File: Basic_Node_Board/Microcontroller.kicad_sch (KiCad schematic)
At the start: 30 parts, among them J1 Conn_01x02, J2 Conn_01x19_Socket, J3 Conn_01x19_Socket, J4 Conn_01x02_Pin, U2 ESP32-DEVKIT-C, U3 AP64060WU-7, U4 AP64060WU-7, U5 AP64060WU-7, U6 TJA1050T/CM,118

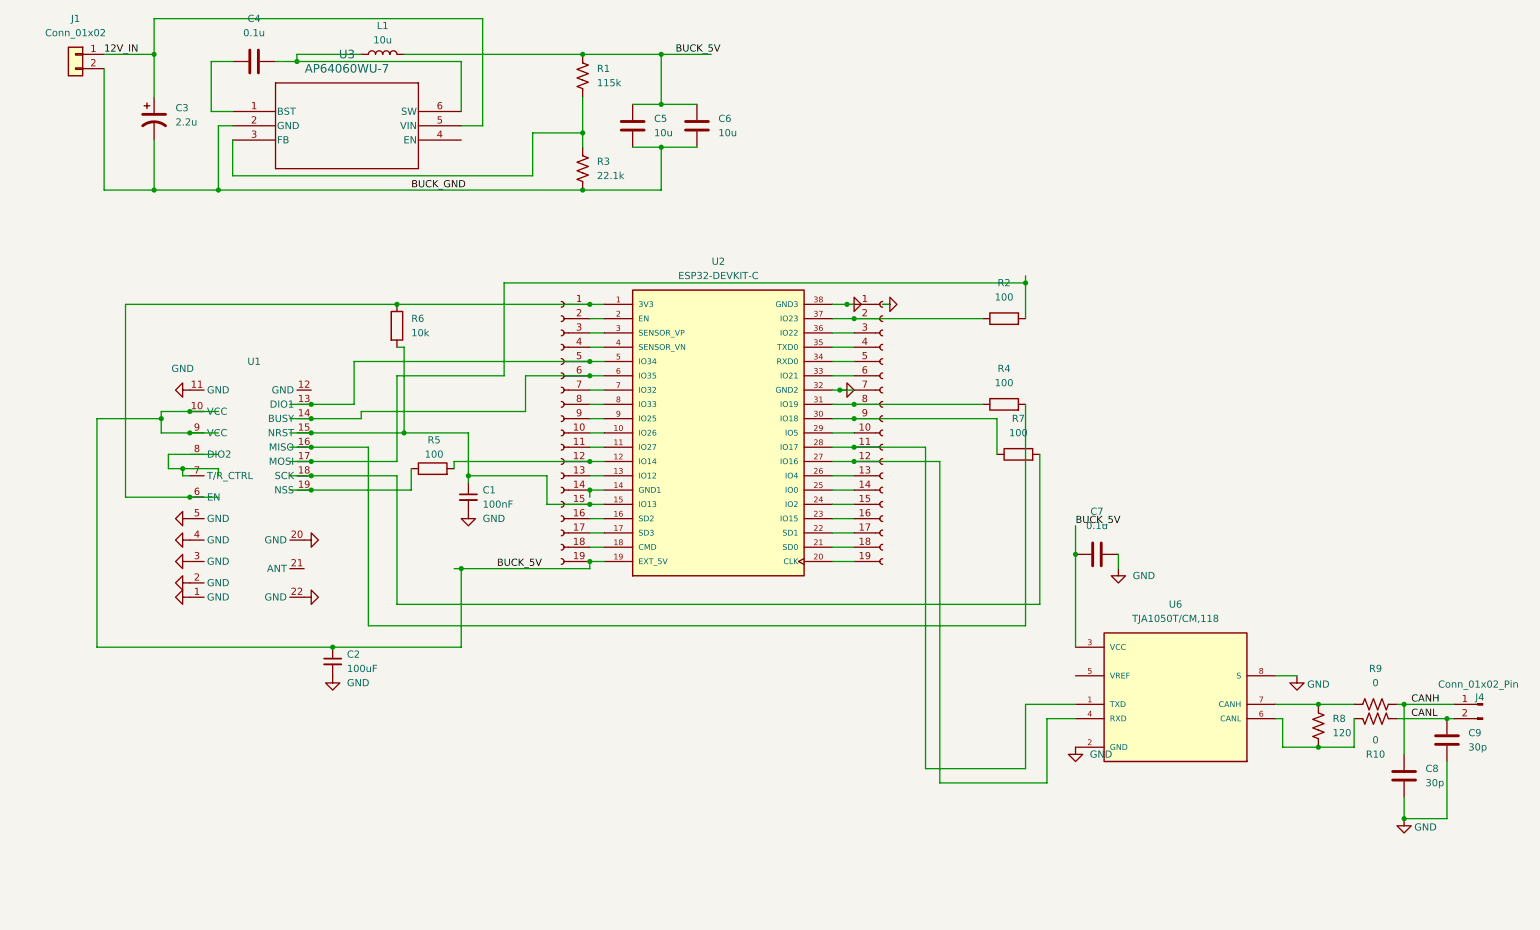
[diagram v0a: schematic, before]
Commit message: microcontroller board without the buck converter yet
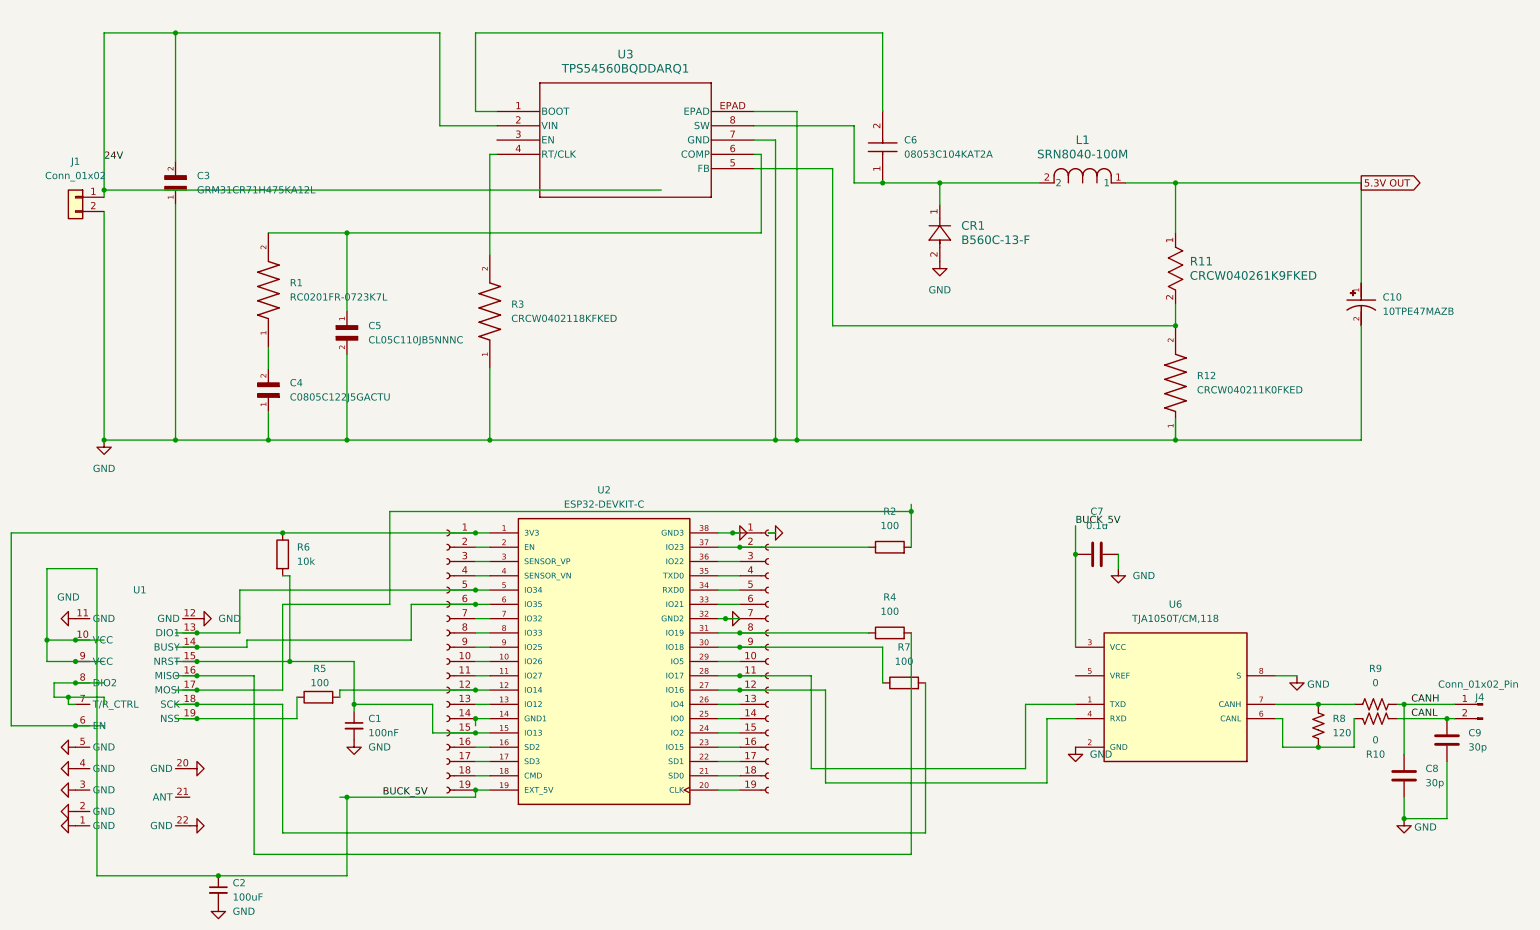
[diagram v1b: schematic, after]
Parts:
- removed C3: 2.2u, Capacitor_SMD:C_1206_3216Metric_Pad1.33x1.80mm_HandSolder, symbol PROVE:EEE-1VA2R2NR
- removed C4: 0.1u, Capacitor_SMD:C_1206_3216Metric_Pad1.33x1.80mm_HandSolder, symbol PROVE:1206B104K500CT
- removed C5, C6: 10u, Capacitor_SMD:C_1206_3216Metric_Pad1.33x1.80mm_HandSolder, symbol PROVE:CL31A106KPHNNNE
- removed L1: 10u, PROVE-footprints:WE-LQS_5040, symbol PROVE:74404054100
- removed R1: 115k, Resistor_SMD:R_1206_3216Metric_Pad1.30x1.75mm_HandSolder, symbol PROVE:RC1206FR-07115KL
- removed R3: 22.1k, Resistor_SMD:R_1206_3216Metric_Pad1.30x1.75mm_HandSolder, symbol PROVE:RNCP1206FTD22K1
- removed U3: AP64060WU-7, Package_TO_SOT_SMD:TSOT-23-6, symbol PROVE:AP64060WU-7
- added C10: 10TPE47MAZB, Capacitor_SMD:C_0402_1005Metric_Pad0.74x0.62mm_HandSolder, symbol 10TPE47MAZB:10TPE47MAZB
- added C3: GRM31CR71H475KA12L, Capacitor_SMD:C_0504_1310Metric_Pad0.83x1.28mm_HandSolder, symbol GRM31CR71H475KA12L:GRM31CR71H475KA12L
- added C4: C0805C122J5GACTU, Capacitor_SMD:C_0504_1310Metric_Pad0.83x1.28mm_HandSolder, symbol C0805C122J5GACTU:C0805C122J5GACTU
- added C5: CL05C110JB5NNNC, Capacitor_SMD:C_0603_1608Metric_Pad1.08x0.95mm_HandSolder, symbol CL05C110JB5NNNC:CL05C110JB5NNNC
- added C6: 08053C104KAT2A, Capacitor_SMD:C_0504_1310Metric_Pad0.83x1.28mm_HandSolder, symbol 08053C104KAT2A:08053C104KAT2A
- added CR1: B560C-13-F, Diode_SMD:D_0201_0603Metric_Pad0.64x0.40mm_HandSolder, symbol B560C-13-F:B560C-13-F
- added L1: SRN8040-100M, Inductor_SMD:L_0201_0603Metric_Pad0.64x0.40mm_HandSolder, symbol SRN8040-100M:SRN8040-100M
- added R1: RC0201FR-0723K7L, Resistor_SMD:R_0201_0603Metric_Pad0.64x0.40mm_HandSolder, symbol RC0201FR-0723K7L:RC0201FR-0723K7L
- added R11: CRCW040261K9FKED, Resistor_SMD:R_0201_0603Metric_Pad0.64x0.40mm_HandSolder, symbol 2026-02-07_22-08-15:CRCW040261K9FKED
- added R12: CRCW040211K0FKED, Resistor_SMD:R_0201_0603Metric_Pad0.64x0.40mm_HandSolder, symbol CRCW040211K0FKED:CRCW040211K0FKED
- added R3: CRCW0402118KFKED, Resistor_SMD:R_0201_0603Metric_Pad0.64x0.40mm_HandSolder, symbol CRCW0402118KFKED:CRCW0402118KFKED
- added U3: TPS54560BQDDARQ1, PROVE-footprints:VREG_LM5017MR_NOPB, symbol TPS54560BQDDARQ1:TPS54560BQDDARQ1
- J1: footprint Connector_PinHeader_1.00mm:PinHeader_1x02_P1.00mm_Horizontal -> Connector_PinHeader_2.54mm:PinHeader_1x04_P2.54mm_Vertical
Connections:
- net BUCK_GND is gone; now on net GND: J1.2 (Pin_2)
- net GND: now also U1.12 (GND), C10.2, C3.1, C4.1, C5.2, CR1.2, R12.1, R3.1, U3.7 (GND), U3.EPAD
- net at U1.7 (T/R_CTRL): now also U1.8 (DIO2)
- net 12V_IN renamed 24V
- net 24V: now also C3.2, U3.2 (VIN)
- new net: R3.2, U3.4 (RT/CLK)
- new net: C6.1, CR1.1, L1.2, U3.8 (SW)
- new net: C4.2, R1.1
- new net: C6.2, U3.1 (BOOT)
- new net: R11.2, R12.2, U3.5 (FB)
- new net: C5.1, R1.2, U3.6 (COMP)
- new net 5.3V OUT: C10.1, L1.1, R11.1
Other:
- moved on the sheet: C1, C2, J1, R2, R4, R5, R6, R7, U1, U2

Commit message: beta test with all connections for final pcb layout - JK
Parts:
- added C11: 47uF, Capacitor_SMD:C_0402_1005Metric_Pad0.74x0.62mm_HandSolder, symbol 10TPE47MAZB:10TPE47MAZB
- C10: value 10TPE47MAZB -> 47uF
- C3: value GRM31CR71H475KA12L -> 30uF
- C4: value C0805C122J5GACTU -> 82nF
- C5: value CL05C110JB5NNNC -> 100pF
- J1: footprint Connector_PinHeader_2.54mm:PinHeader_1x04_P2.54mm_Vertical -> Connector_PinHeader_1.00mm:PinHeader_1x02_P1.00mm_Vertical
- L1: value SRN8040-100M -> 47uH
- R1: value RC0201FR-0723K7L -> 5.1k
- R11: value CRCW040261K9FKED -> 10k
- R12: value CRCW040211K0FKED -> 56.2k
- R3: value CRCW0402118KFKED -> 243k
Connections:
- net BUCK_5V is gone; now on net 5.3V OUT: C2.1, C7.2, J2.19 (Pin_19), U1.10 (VCC), U1.9 (VCC), U2.19 (EXT_5V), U6.3 (VCC)
- net 24V: now also U3.3 (EN)
- net 5.3V OUT: now also R12.2, C11.1; no longer R11.1
- net GND: now also R11.2, C11.2; no longer R12.1
- new net: R11.1, R12.1, U3.5 (FB)
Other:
- moved on the sheet: C10, R11, R12

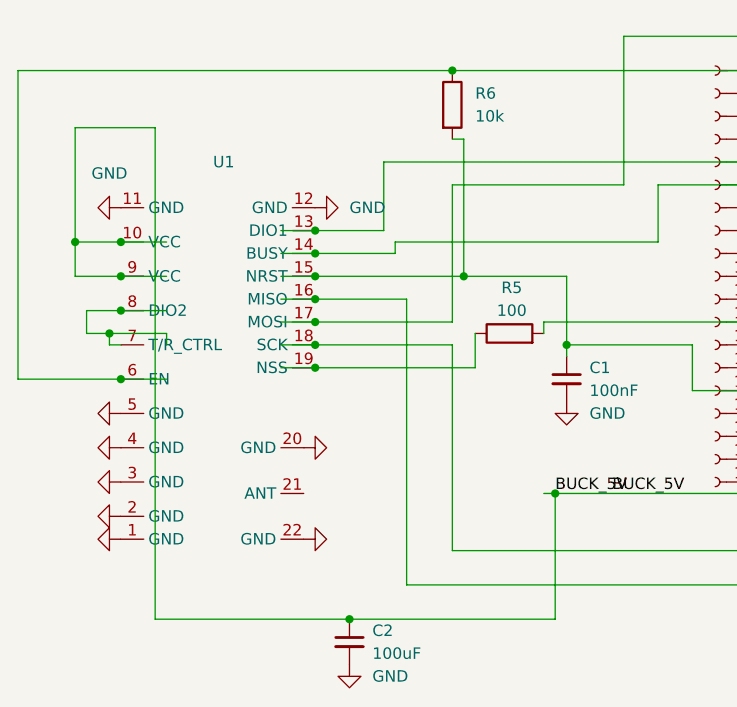
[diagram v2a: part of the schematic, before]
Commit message: revised e22P transceiver module footprint and began to add labels for the 3d Board design
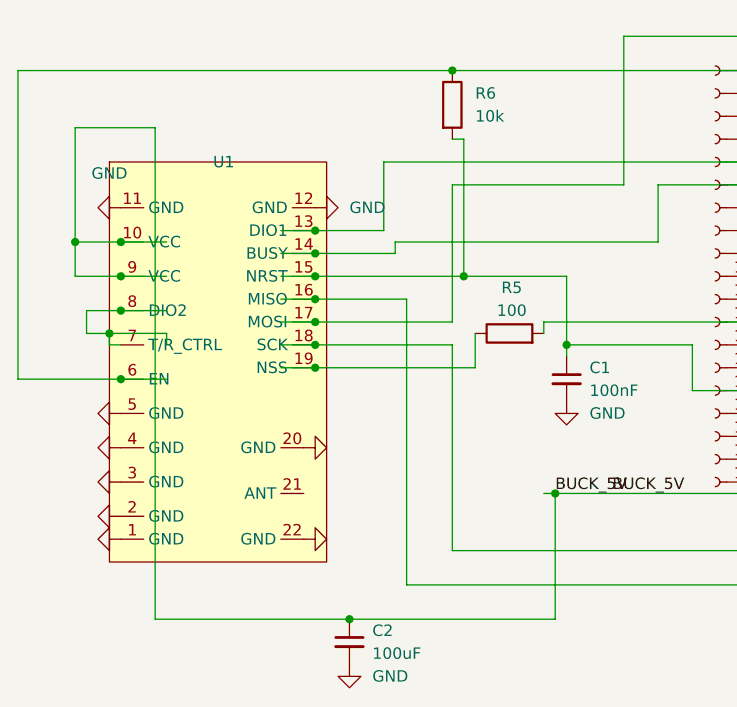
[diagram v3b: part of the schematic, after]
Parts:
- J1, J4: footprint Connector_PinHeader_1.00mm:PinHeader_1x02_P1.00mm_Vertical -> Connector_PinSocket_1.00mm:PinSocket_1x02_P1.00mm_Vertical
- U1: footprint Library:E22P-915M30S -> PROVE-footprints:E22P-915M30S_revised
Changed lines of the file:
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@@
 			)
 		)
-		(property "Footprint" "Library:E22P-915M30S"
+		(property "Footprint" "PROVE-footprints:E22P-915M30S_revised"
 			(at 38.1 120.65 0)
 			(effects
@@
 			)
 		)
-		(property "Footprint" "Connector_PinHeader_1.00mm:PinHeader_1x02_P1.00mm_Vertical"
+		(property "Footprint" "Connector_PinSocket_1.00mm:PinSocket_1x02_P1.00mm_Vertical"
 			(at 26.67 49.53 0)
 			(effects
@@
 			)
 		)
-		(property "Footprint" "Connector_PinHeader_1.00mm:PinHeader_1x02_P1.00mm_Vertical"
+		(property "Footprint" "Connector_PinSocket_1.00mm:PinSocket_1x02_P1.00mm_Vertical"
 			(at 276.86 139.7 0)
 			(effects
